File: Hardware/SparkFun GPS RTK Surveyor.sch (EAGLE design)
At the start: 94 parts, among them J16 microSD, J3 USB-C, J4 Qwiic Right Angle, J6 Start Base, J7 Power Switch, Q2 MBT3904DW1T1, U1 MCP73831, U2 3.3V, U3 U-BLOX_ZED-F9P, U5 ESP-WROOM-32NARROW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

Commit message: v13 hardware. Fix power LED. Add gcode for enclosure.
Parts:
- removed B1: 6.8MM_COIN_CELL, SparkFun-Batteries:ML414H_IV01E_BATTERY
- removed C3: 1.0uF, SparkFun-Capacitors:1.0UF-0603-16V-10%-X7R
- removed D13: RGB, SparkFun-LED:LED-RGB-CAPLCC
- removed D2: 0.5A/40V/420mV, SparkFun-DiscreteSemi:DIODE-SCHOTTKY-PMEG4005EJ
- removed R5: 3.3k, SparkFun-Resistors:3.3KOHM-0603-1/10W-1%
- removed S1: RESET, SparkFun-Switches:MOMENTARY-SWITCH-SPST-SMD-5.2-TALL-REDUNDANT
- added C17, C18: 1.0uF, SparkFun-Capacitors:1.0UF-0603-16V-10%-X7R
- added D5: RGB, SparkFun-LED:LED-RGBPLCC-6
- added R1: 1k, SparkFun-Resistors:1KOHM-0603-1/10W-1%
- added R6, R8: 330, SparkFun-Resistors:330OHM-0603-1/10W-1%
- added U4: 3.3V, SparkFun-IC-Power:V_REG_AP2112K-3.3V
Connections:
- removed net ESP_32: J14.2, U5.XTAL_P/IO32
- removed net ESP_33: J14.1, U5.XTAL_N/IO33
- removed net ESP_34/PWR_LVL_RED: D13.RED, U5.IO34
- removed net ESP_35/PWR_LVL_GRN: D13.GRN, U5.IO35
- removed net N$6: D2.C, R5.2
- new net ESP_32/PWR_LVL_RED: D5.RED-A, U5.XTAL_P/IO32
- new net ESP_33/PWR_LVL_GRN: D5.GRN-A, U5.XTAL_N/IO33
- new net ESP_I34: U5.I34
- new net ESP_I35: U5.I35
- new net N$10: D5.GRN-C, R6.1
- new net N$14: D5.RED-C, R8.1
- new net N$17: D5.BLU-C, R1.1
- net 3.3V: no longer D2.A
- net BACKUP: now also C18.1, U4.OUT; no longer B1.+, C3.1, R5.1
- net CHG_LED: now also R1.2; no longer D13.BLU
- net ESP32_EN: now also J14.1; no longer S1.2
- net ESP_16/BT_RXI: now also BLUETOOTH_BROADCAST.2; no longer BLUETOOTH_BROADCAST.5
- net ESP_17/BT_TXO: now also BLUETOOTH_BROADCAST.5; no longer BLUETOOTH_BROADCAST.2
- net EXTERNAL_SERIAL1_RXI: now also SERIAL1_CONNECTION.4; no longer SERIAL1_CONNECTION.3
- net EXTERNAL_SERIAL1_TXO: now also SERIAL1_CONNECTION.1; no longer SERIAL1_CONNECTION.6
- net GND: now also C17.2, C18.2, J14.2, R6.2, R8.2, U4.GND; no longer B1.-, C3.2, S1.1
- net NMEA-RX: now also BLUETOOTH_BROADCAST.6, SERIAL1_CONNECTION.6; no longer BLUETOOTH_BROADCAST.1, SERIAL1_CONNECTION.1
- net NMEA-TX: now also BLUETOOTH_BROADCAST.3, SERIAL1_CONNECTION.3; no longer BLUETOOTH_BROADCAST.4, SERIAL1_CONNECTION.4
- net VIN: now also D5.BLU-A; no longer D13.A
- net V_BATT: now also C17.1, U4.EN, U4.IN
- net ZED-RXI1: now also SERIAL1_CONNECTION.5; no longer SERIAL1_CONNECTION.2
- net ZED-RXI2: now also BLUETOOTH_BROADCAST.4; no longer BLUETOOTH_BROADCAST.3
- net ZED-TXO1: now also SERIAL1_CONNECTION.2; no longer SERIAL1_CONNECTION.5
- net ZED-TXO2: now also BLUETOOTH_BROADCAST.1; no longer BLUETOOTH_BROADCAST.6
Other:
- note added: "Ext Cntr"
- note removed: "Add MEAS jumper to batt"
- note removed: "Add batt level leds"
- note removed: "Add fuel guage"
- note removed: "Move ESP32 USB to panel edge"
- note removed: "Move Qwiic connector"
- note removed: "Move microSD to panel edge"
- moved on the sheet: BLUETOOTH_BROADCAST, D1, D3, J14, R11, R12, SERIAL1_CONNECTION

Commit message: Change resistor values on LEDs to try to balance brightness.
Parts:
- J3: value USB-C -> ESP32 USB
- J5: value (none) -> u-blox USB
- R1: value 1k -> 4.7k; device SparkFun-Resistors:1KOHM-0603-1/10W-1% -> SparkFun-Resistors:4.7KOHM-0603-1/10W-1%
- R11, R24, R25, R26: value 330 -> 20; device SparkFun-Resistors:330OHM-0603-1/10W-1% -> SparkFun-Resistors:20OHM-0603-1/10W-1%
- R6, R8: value 330 -> 1k; device SparkFun-Resistors:330OHM-0603-1/10W-1% -> SparkFun-Resistors:1KOHM-0603-1/10W-1%
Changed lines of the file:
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@@
 <part name="GND4" library="SparkFun-PowerSymbols" deviceset="GND" device=""/>
 <part name="D1" library="SparkFun-LED" deviceset="LED-YELLOW" device="0603" value="Yellow"/>
-<part name="R11" library="SparkFun-Resistors" deviceset="330OHM" device="-0603-1/10W-1%" value="330"/>
+<part name="R11" library="SparkFun-Resistors" deviceset="20OHM" device="-0603-1/10W-1%" value="20"/>
 <part name="JP71" library="SparkFun-Aesthetics" deviceset="FIDUCIAL" device="UFIDUCIAL" value="FIDUCIALUFIDUCIAL"/>
 <part name="JP81" library="SparkFun-Aesthetics" deviceset="FIDUCIAL" device="UFIDUCIAL" value="FIDUCIALUFIDUCIAL"/>
@@
 <part name="R16" library="SparkFun-Resistors" deviceset="5.1KOHM" device="5.1KOHM-0603-1/10W-1%" value="5.1k"/>
 <part name="R17" library="SparkFun-Resistors" deviceset="5.1KOHM" device="5.1KOHM-0603-1/10W-1%" value="5.1k"/>
-<part name="J5" library="SparkFun-Connectors" deviceset="USB_C" device="_2-LAYER_PADS"/>
+<part name="J5" library="SparkFun-Connectors" deviceset="USB_C" device="_2-LAYER_PADS" value="u-blox USB"/>
 <part name="U$2" library="SparkFun-Aesthetics" deviceset="SPECIAL_INSTRUCTIONS" device="-ORDERING"/>
 <part name="C2" library="SparkFun-Capacitors" deviceset="1.0UF" device="-0603-16V-10%-X7R" value="1.0uF"/>
@@
 <part name="GND12" library="SparkFun-PowerSymbols" deviceset="GND" device=""/>
 <part name="D7" library="SparkFun-DiscreteSemi" deviceset="DIODE-SCHOTTKY" device="-BAT60A" value="3A/10V/280mV"/>
-<part name="R24" library="SparkFun-Resistors" deviceset="330OHM" device="-0603-1/10W-1%" value="330"/>
+<part name="R24" library="SparkFun-Resistors" deviceset="20OHM" device="-0603-1/10W-1%" value="20"/>
 <part name="D8" library="SparkFun-LED" deviceset="LED-GREEN" device="0603" value="GREEN"/>
 <part name="GND20" library="SparkFun-PowerSymbols" deviceset="GND" device=""/>
-<part name="R25" library="SparkFun-Resistors" deviceset="330OHM" device="-0603-1/10W-1%" value="330"/>
+<part name="R25" library="SparkFun-Resistors" deviceset="20OHM" device="-0603-1/10W-1%" value="20"/>
 <part name="D10" library="SparkFun-LED" deviceset="LED-GREEN" device="0603" value="GREEN"/>
 <part name="GND21" library="SparkFun-PowerSymbols" deviceset="GND" device=""/>
-<part name="R26" library="SparkFun-Resistors" deviceset="330OHM" device="-0603-1/10W-1%" value="330"/>
+<part name="R26" library="SparkFun-Resistors" deviceset="20OHM" device="-0603-1/10W-1%" value="20"/>
 <part name="D11" library="SparkFun-LED" deviceset="LED-GREEN" device="0603" value="GREEN"/>
 <part name="GND22" library="SparkFun-PowerSymbols" deviceset="GND" device=""/>
@@
 <part name="R29" library="SparkFun-Resistors" deviceset="10KOHM" device="-0603-1/10W-1%" value="10k"/>
 <part name="Q2" library="SparkFun-DiscreteSemi" deviceset="TRANS_NPN_DUAL" device="-MBT3904DW1T1" value="MBT3904DW1T1"/>
-<part name="J3" library="SparkFun-Connectors" deviceset="USB_C" device="_2-LAYER_PADS" value="USB-C"/>
+<part name="J3" library="SparkFun-Connectors" deviceset="USB_C" device="_2-LAYER_PADS" value="ESP32 USB"/>
 <part name="R37" library="SparkFun-Resistors" deviceset="5.1KOHM" device="5.1KOHM-0603-1/10W-1%" value="5.1k"/>
 <part name="R38" library="SparkFun-Resistors" deviceset="5.1KOHM" device="5.1KOHM-0603-1/10W-1%" value="5.1k"/>
@@
 <part name="D5" library="SparkFun-LED" deviceset="LED-RGB" device="PLCC-6" value="RGB"/>
 <part name="SUPPLY24" library="SparkFun-PowerSymbols" deviceset="VIN" device=""/>
-<part name="R1" library="SparkFun-Resistors" deviceset="1KOHM" device="-0603-1/10W-1%" value="1k"/>
-<part name="R6" library="SparkFun-Resistors" deviceset="330OHM" device="-0603-1/10W-1%" value="330"/>
-<part name="R8" library="SparkFun-Resistors" deviceset="330OHM" device="-0603-1/10W-1%" value="330"/>
+<part name="R1" library="SparkFun-Resistors" deviceset="4.7KOHM" device="-0603-1/10W-1%" value="4.7k"/>
+<part name="R6" library="SparkFun-Resistors" deviceset="1KOHM" device="-0603-1/10W-1%" value="1k"/>
+<part name="R8" library="SparkFun-Resistors" deviceset="1KOHM" device="-0603-1/10W-1%" value="1k"/>
 <part name="GND37" library="SparkFun-PowerSymbols" deviceset="GND" device=""/>
 <part name="U4" library="SparkFun-IC-Power" deviceset="V_REG_AP2112" device="K-3.3V" value="3.3V"/>
@@
 </instance>
 <instance part="J3" gate="J1" x="279.4" y="231.14" smashed="yes">
+<attribute name="VALUE" x="276.86" y="218.694" size="1.778" layer="96" font="vector" rot="MR180" align="top-left"/>
 <attribute name="NAME" x="276.86" y="241.554" size="1.778" layer="95" font="vector"/>
 </instance>
@@
 </nets>
 </sheet>
-<sheet>
-<plain>
-</plain>
-<instances>
-</instances>
-<busses>
-</busses>
-<nets>
-</nets>
-</sheet>

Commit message: Add ESD protection to ESP USB. Change charge IC with 42C temp limit. Reroute ZED USB.
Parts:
- removed U1: MCP73831, SparkFun-IC-Power:MCP73831
- added D2: PRTR5V0U2F, SparkFun-IC-Power:PRTR5V0U2F
- added FRAME1: FRAME-LETTERNO_PACKAGE, SparkFun-Aesthetics:FRAME-LETTERNO_PACKAGE
- added R18: 10k, SparkFun-Resistors:NTC-THERMISTOR-0603
- added R30: 150k, SparkFun-Resistors:150KOHM-0603-1/10W-1%
- added R5: 0, SparkFun-Resistors:0OHM-0603-1/10W
- added U10: MCP73833, SparkFun-IC-Power:MCP73833
- E1: device SparkFun-RF:ANTENNA-GROUNDEDEDGE_SMA_SMD -> SparkFun-RF:ANTENNA-SMA-GROUNDEDEDGE_SMA_SMD
- J3: value ESP32 USB -> USB Female Type C Connector; device SparkFun-Connectors:USB_C_2-LAYER_PADS -> SparkFun-Connectors:USB_C_4-LAYER_PADS
- J5: value u-blox USB -> USB Female Type C Connector; device SparkFun-Connectors:USB_C_2-LAYER_PADS -> SparkFun-Connectors:USB_C_4-LAYER_PADS
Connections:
- net N$7 renamed LIPO_RAW
- new net CHG_THERM1: R18.2, R30.2, R5.2
- new net ESP_D1+: D2.3, J3.D+
- new net ESP_D1-: D2.1, J3.D-
- new net PROG1: R7.2, U10.PROG
- net CHG_LED: now also U10.STAT1; no longer U1.STAT
- net D+1: now also D2.4; no longer J3.D+
- net D-1: now also D2.6; no longer J3.D-
- net GND: now also D2.2, R18.1, R30.1, U10.VSS; no longer U1.VSS
- net N$5: now also R5.1, U10.THERM; no longer R7.2, U1.PROG
- net VIN: now also D2.5, U10.VDD; no longer U1.VIN
- net V_BATT: now also U10.VBAT; no longer U1.VBAT
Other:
- note added: "10k, +/-5%, B-Constant 3380"
- note added: "LiPo Charger @ 1A"
- note added: "NCP18XH103J03RB"
- note added: "Temp Cutoff: 0C to 42C"
- note added: "USB For ZED-F9P Power Switch"
- note added: "Use with >1Ahr 3.7V Battery"
- note added: "v13"
- note removed: "LiPo Charger"
- note removed: "USB / Power"
- note removed: "v12"

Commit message: Rename Binaries folder. Combine binary into one. Update readmes.
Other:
- note added: "N. Seidle"
- moved on the sheet: J1, J11, J12, J13, J2, J4, J9

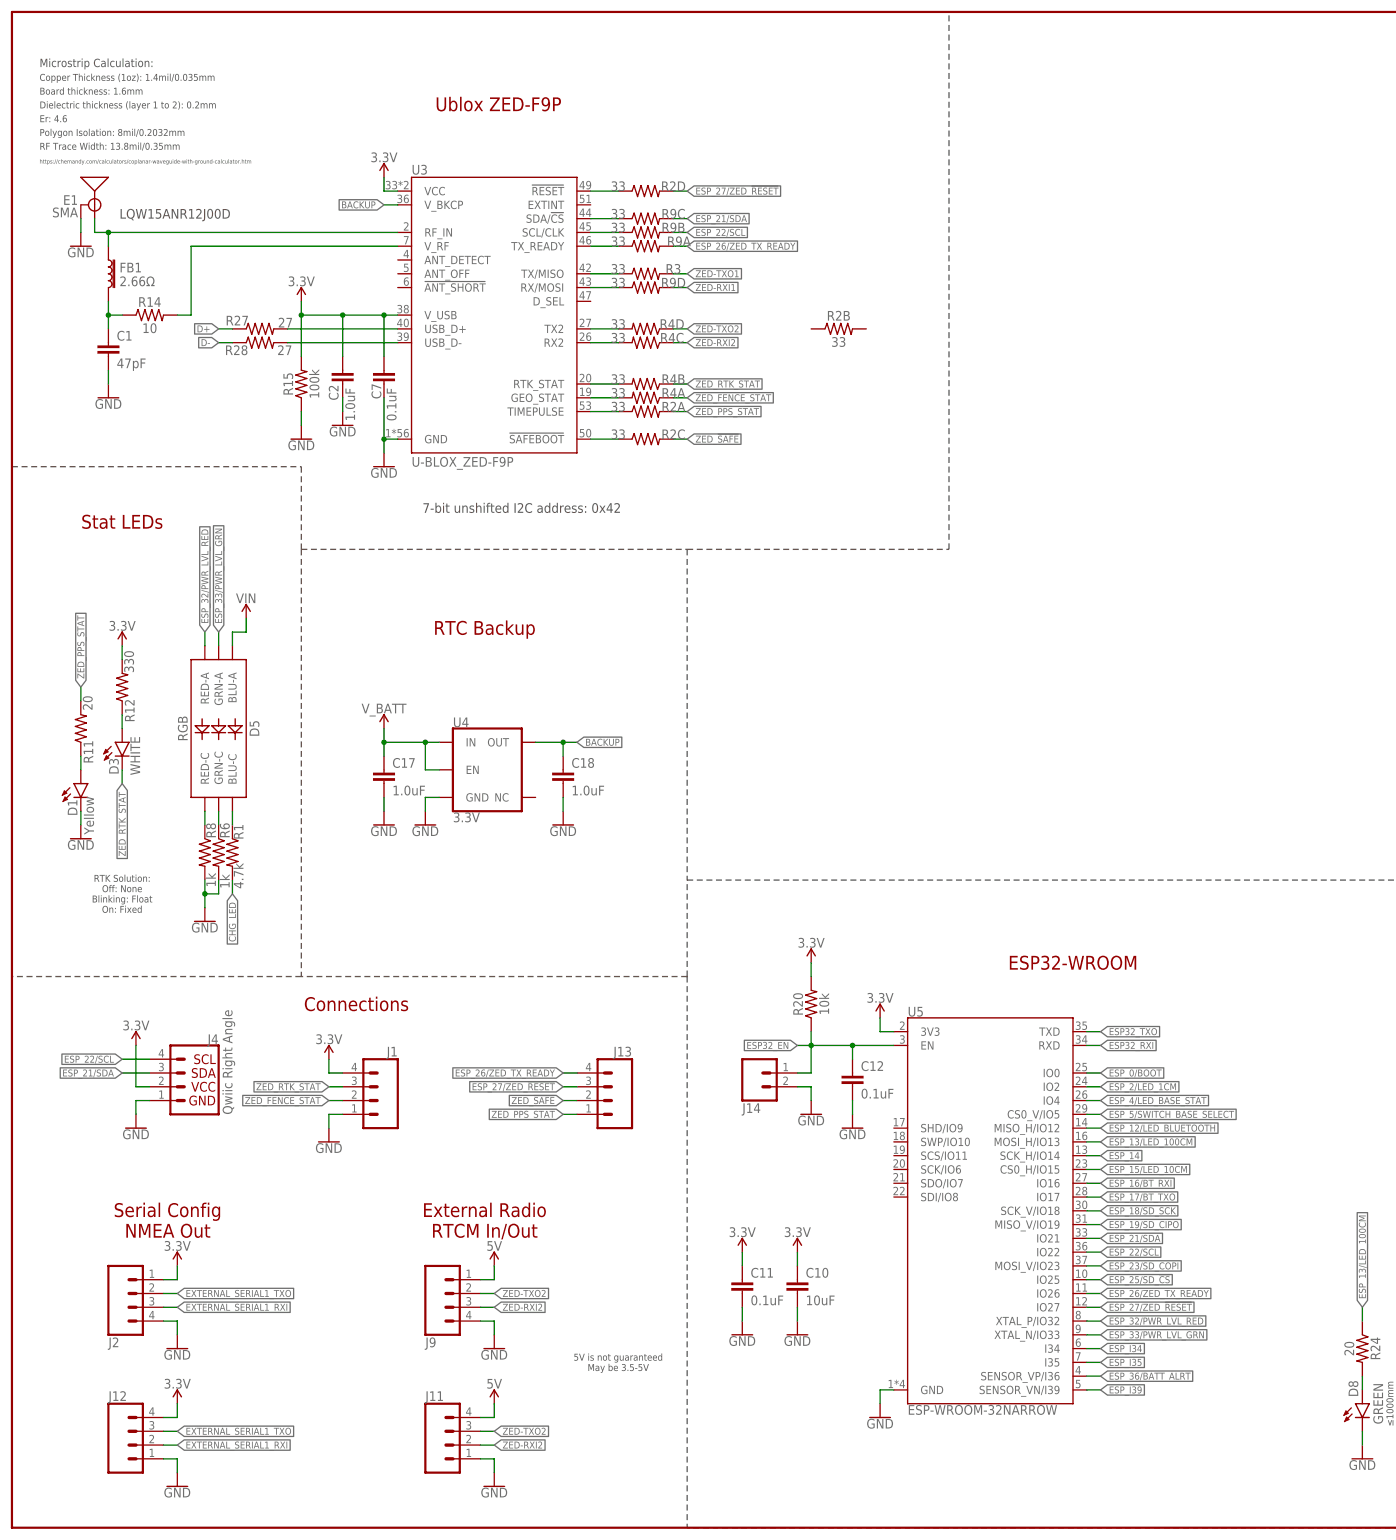
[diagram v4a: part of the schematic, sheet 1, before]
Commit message: v1.5: Add I2C and D_SEL PTH connections.
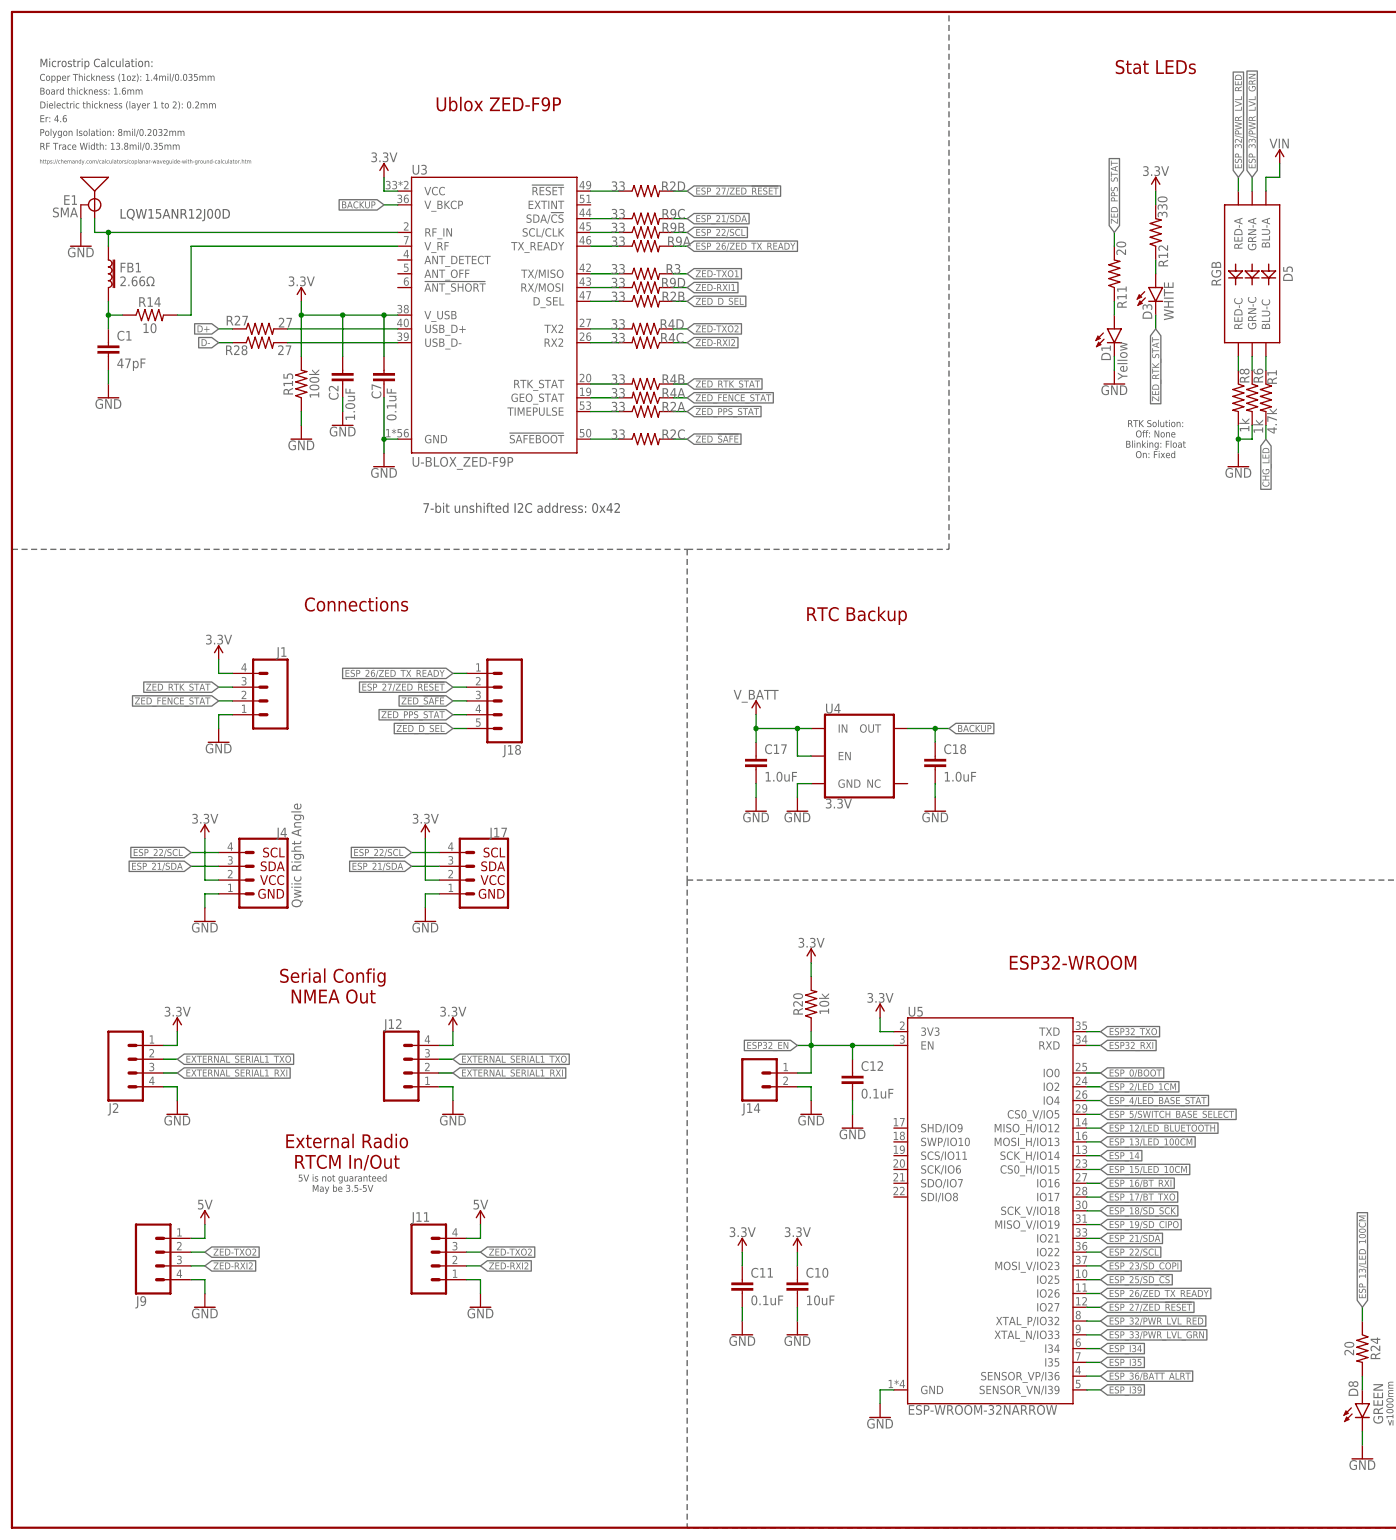
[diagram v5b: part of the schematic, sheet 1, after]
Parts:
- removed J13: (no value), SparkFun-Connectors:CONN_041X04_NO_SILK_NO_POP
- added J17: Qwiic Right Angle, SparkFun-Connectors:I2C_STANDARD_NO_SILK
- added J18: (no value), SparkFun-Connectors:CONN_05NO_SILK
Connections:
- net N$16 renamed ESP_27/ZED_!RESET!_LV
- net N$18 renamed ZED_!SAFE!_LV
- net N$22 renamed ESP_26/ZED_TX_READY_LV
- new net ZED_D_SEL: J18.5, R2B.2
- new net ZED_D_SEL_LV: R2B.1, U3.D_SEL
- net 3.3V: now also J17.2
- net ESP_21/SDA: now also J17.3
- net ESP_22/SCL: now also J17.4
- net ESP_26/ZED_TX_READY: now also J18.1; no longer J13.4
- net ESP_27/ZED_!RESET!: now also J18.2; no longer J13.3
- net GND: now also J17.1
- net ZED_!SAFE!: now also J18.3; no longer J13.2
- net ZED_PPS_STAT: now also J18.4; no longer J13.1
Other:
- moved on the sheet: C17, C18, D1, D3, D5, J1, J11, J12, J2, J4, J9, R1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
